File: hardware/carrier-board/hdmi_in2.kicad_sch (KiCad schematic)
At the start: 0 parts

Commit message: Integrate real downloaded component libraries; place first symbols
User downloaded SnapEDA exports for TXS0102DCUR and SS5-80-3.50-L-D-K-TR
(the level translator and SOM B2B connector selected in
carrier-board-spec.md). Extracted into hardware/carrier-board/libs/
(symbols, footprints, STEP models), re-validated every symbol and
footprint through kicad-cli sym/fp upgrade before trusting them, and
wired them into the project via sym-lib-table/fp-lib-table (with
name-aliased footprint entries matching what's baked into each
downloaded symbol's Footprint property).

Placed TXS0102DCUR in all 4 relevant sheets (hdmi_in1-3, hdmi_out) --
caught and fixed a real bug in the process (nested sub-symbol name
needs the bare "PART_0_0" form, not "LIB:PART_0_0" -- the first attempt
failed to load entirely). Also fixed grid-off-placement and a
lib_symbol_mismatch (embedded copies were missing several properties
present in the source library) once ERC surfaced them. Full-hierarchy
ERC now shows only expected "pin not connected" warnings across all
4 sheets -- correct for placed-but-unwired components, no structural
errors.

Placed J1 of the SS5 connector (160 pins, 2-unit symbol) in
som_connector.kicad_sch. Hit a real, narrower limit here: kicad-cli's
non-interactive upgrade collapses both unit instances to "unit 1"
during normalization. Verified this doesn't lose or duplicate any pin
data (160 unique pins, correctly mapped) -- it's a cosmetic/organizational
quirk in headless multi-unit handling, not a netlist bug -- but
couldn't resolve it further without the interactive GUI's purpose-built
multi-unit placement tools. Flagged in the README for the user to check
in real KiCad before J2-J4 get placed the same way.

Si5341A, ESD8040, and the Amphenol HDMI connector still need
hand-transcription from datasheets -- no pre-made libraries found for
those. README updated with full current status and next steps.
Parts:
- added U1: TXS0102DCUR, TXS0102DCUR:SOP50P310X90-8N, symbol TXS0102DCUR:TXS0102DCUR
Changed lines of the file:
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@@
 		(title "OpenAVSwitch Carrier Board - HDMI Input 2")
 		(company "OpenAVSwitch")
-		(comment 1 "Stub sheet -- not yet populated, see docs/carrier-board-spec.md")
+		(comment 1 "DDC/HPD level translator placed (TXS0102DCUR). TMDS/connector/ESD/EDID still to add.")
+	)
+	(symbol
+		(lib_id "TXS0102DCUR:TXS0102DCUR")
+		(at 99.06 99.06 0)
+		(unit 1)
+		(body_style 1)
+		(exclude_from_sim no)
+		(in_bom yes)
+		(on_board yes)
+		(in_pos_files yes)
+		(dnp no)
+		(property "Reference" "U1"
+			(at 100 80 0)
+			(show_name no)
+			(do_not_autoplace no)
+			(effects
+				(font
+					(size 1.27 1.27)
+				)
+			)
+		)
+		(property "Value" "TXS0102DCUR"
+			(at 100 122 0)
+			(show_name no)
+			(do_not_autoplace no)
+			(effects
+				(font
+					(size 1.27 1.27)
+				)
+			)
+		)
+		(property "Footprint" "TXS0102DCUR:SOP50P310X90-8N"
+			(at 99.06 99.06 0)
+			(hide yes)
+			(show_name no)
+			(do_not_autoplace no)
+			(effects
+				(font
+					(size 1.27 1.27)
+				)
+			)
+		)
+		(property "Datasheet" ""
+			(at 99.06 99.06 0)
+			(show_name no)
+			(do_not_autoplace no)
+			(effects
+				(font
+					(size 1.27 1.27)
+				)
+			)
+		)
+		(property "Description" ""
+			(at 99.06 99.06 0)
+			(show_name no)
+			(do_not_autoplace no)
+			(effects
+				(font
+					(size 1.27 1.27)
+				)
+			)
+		)
+		(pin "1"
+		)
+		(pin "2"
+		)
+		(pin "3"
+		)
+		(pin "4"
+		)
+		(pin "5"
+		)
+		(pin "6"
+		)
+		(pin "7"
+		)
+		(pin "8"
+		)
 	)
 	(sheet_instances

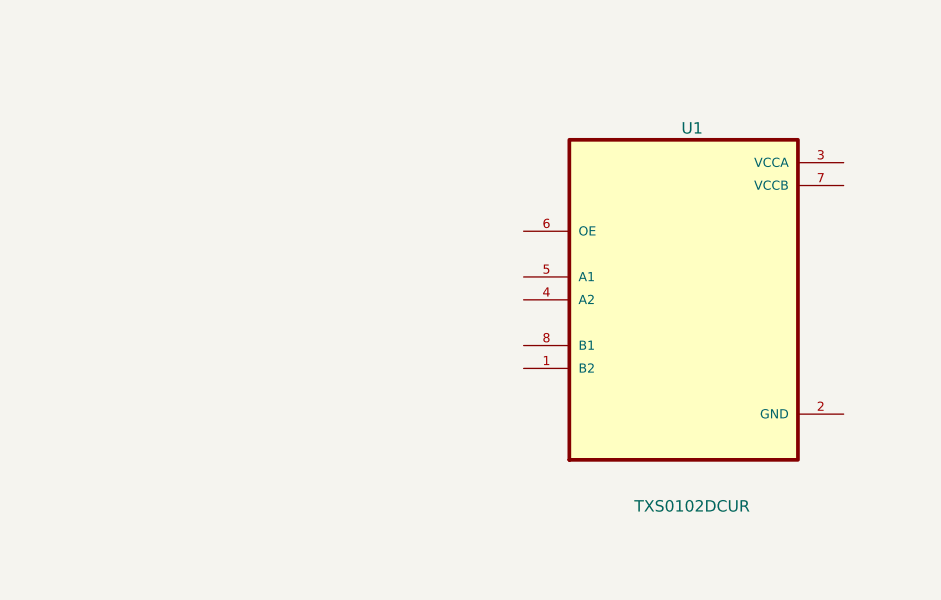
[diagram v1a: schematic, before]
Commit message: Place HDMI connector and wire TXS0102 power pins in all 4 HDMI sheets
Adds the resolved HDMI_TypeA_Receptacle (real Amphenol footprint) to
hdmi_in1-3/hdmi_out, and wires each TXS0102DCUR's VCCA/VCCB/GND to
+3V3/GND via global labels (same label-coincidence technique used in
power.kicad_sch).

Caught and fixed a real bug along the way: the local-to-global pin
coordinate transform needs global_y = base_y - local_y (KiCad flips
symbol-editor Y on placement), not +. Getting it backwards silently
swapped which net the GND and VCCB pins joined instead of failing
loudly. Also documents a kicad-cli sch erc engine quirk (traversal-
order false positive on HDMI Input 1's VCCA/GND, isolated by swapping
sheet-file references) that is not a real wiring defect.
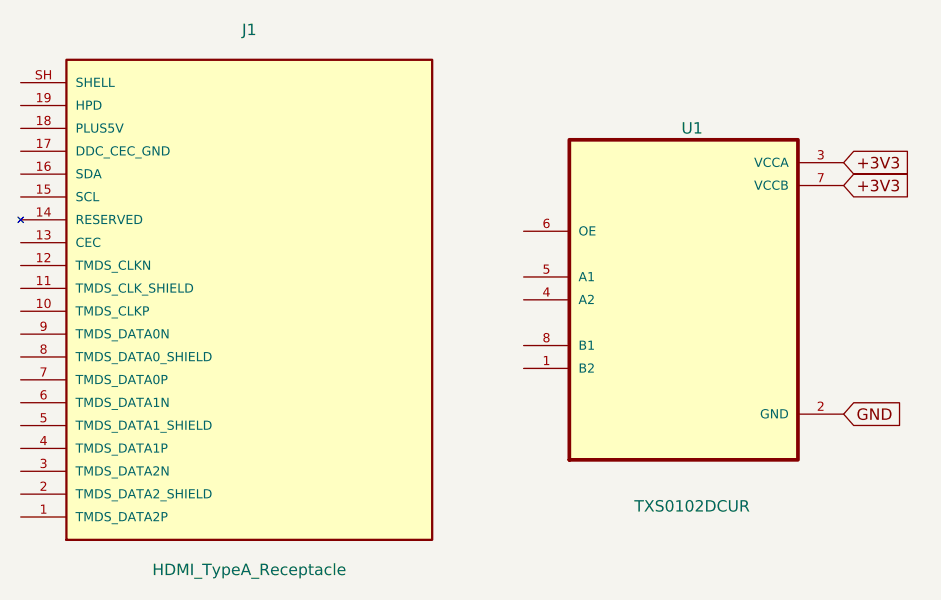
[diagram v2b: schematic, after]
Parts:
- added J1: HDMI_TypeA_Receptacle, carrier_footprints:HDMI_A_Amphenol_10029449-x01xLF_Horizontal, symbol HDMI_TypeA_Receptacle:HDMI_TypeA_Receptacle
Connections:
- net GND: now reaches U1.2 (GND)
- net +3V3: now reaches U1.3 (VCCA)
- net +3V3: now also U1.7 (VCCB)
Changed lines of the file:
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@@
 		(comment 1 "DDC/HPD level translator placed (TXS0102DCUR). TMDS/connector/ESD/EDID still to add.")
+	)
+	(global_label "GND"
+		(shape input)
+		(at 116.84 111.76 0)
+		(fields_autoplaced yes)
+		(effects
+			(font
+				(size 1.27 1.27)
+			)
+			(justify left)
+		)
+		(property "Intersheetrefs" "${INTERSHEET_REFS}"
+			(at 116.84 111.76 0)
+			(hide yes)
+			(show_name no)
+			(do_not_autoplace no)
+			(effects
+				(font
+					(size 1.27 1.27)
+				)
+			)
+		)
+	)
+	(global_label "+3V3"
+		(shape input)
+		(at 116.84 83.82 0)
+		(fields_autoplaced yes)
+		(effects
+			(font
+				(size 1.27 1.27)
+			)
+			(justify left)
+		)
+		(property "Intersheetrefs" "${INTERSHEET_REFS}"
+			(at 116.84 83.82 0)
+			(hide yes)
+			(show_name no)
+			(do_not_autoplace no)
+			(effects
+				(font
+					(size 1.27 1.27)
+				)
+			)
+		)
+	)
+	(global_label "+3V3"
+		(shape input)
+		(at 116.84 86.36 0)
+		(fields_autoplaced yes)
+		(effects
+			(font
+				(size 1.27 1.27)
+			)
+			(justify left)
+		)
+		(property "Intersheetrefs" "${INTERSHEET_REFS}"
+			(at 116.84 86.36 0)
+			(hide yes)
+			(show_name no)
+			(do_not_autoplace no)
+			(effects
+				(font
+					(size 1.27 1.27)
+				)
+			)
+		)
 	)
 	(symbol
@@
 		)
 	)
+	(symbol
+		(lib_id "HDMI_TypeA_Receptacle:HDMI_TypeA_Receptacle")
+		(at 50.8 99.06 0)
+		(unit 1)
+		(body_style 1)
+		(exclude_from_sim no)
+		(in_bom yes)
+		(on_board yes)
+		(in_pos_files yes)
+		(dnp no)
+		(property "Reference" "J1"
+			(at 50.8 69.06 0)
+			(show_name no)
+			(do_not_autoplace no)
+			(effects
+				(font
+					(size 1.27 1.27)
+				)
+			)
+		)
+		(property "Value" "HDMI_TypeA_Receptacle"
+			(at 50.8 129.06 0)
+			(show_name no)
+			(do_not_autoplace no)
+			(effects
+				(font
+					(size 1.27 1.27)
+				)
+			)
+		)
+		(property "Footprint" "carrier_footprints:HDMI_A_Amphenol_10029449-x01xLF_Horizontal"
+			(at 50.8 99.06 0)
+			(hide yes)
+			(show_name no)
+			(do_not_autoplace no)
+			(effects
+				(font
+					(size 1.27 1.27)
+				)
+			)
+		)
+		(property "Datasheet" ""
+			(at 50.8 99.06 0)
+			(show_name no)
+			(do_not_autoplace no)
+			(effects
+				(font
+					(size 1.27 1.27)
+				)
+			)
+		)
+		(property "Description" ""
+			(at 50.8 99.06 0)
+			(show_name no)
+			(do_not_autoplace no)
+			(effects
+				(font
+					(size 1.27 1.27)
+				)
+			)
+		)
+		(pin "1"
+		)
+		(pin "2"
+		)
+		(pin "3"
+		)
+		(pin "4"
+		)
+		(pin "5"
+		)
+		(pin "6"
+		)
+		(pin "7"
+		)
+		(pin "8"
+		)
+		(pin "9"
+		)
+		(pin "10"
+		)
+		(pin "11"
+		)
+		(pin "12"
+		)
+		(pin "13"
+		)
+		(pin "14"
+		)
+		(pin "15"
+		)
+		(pin "16"
+		)
+		(pin "17"
+		)
+		(pin "18"
+		)
+		(pin "19"
+		)
+		(pin "SH"
+		)
+	)

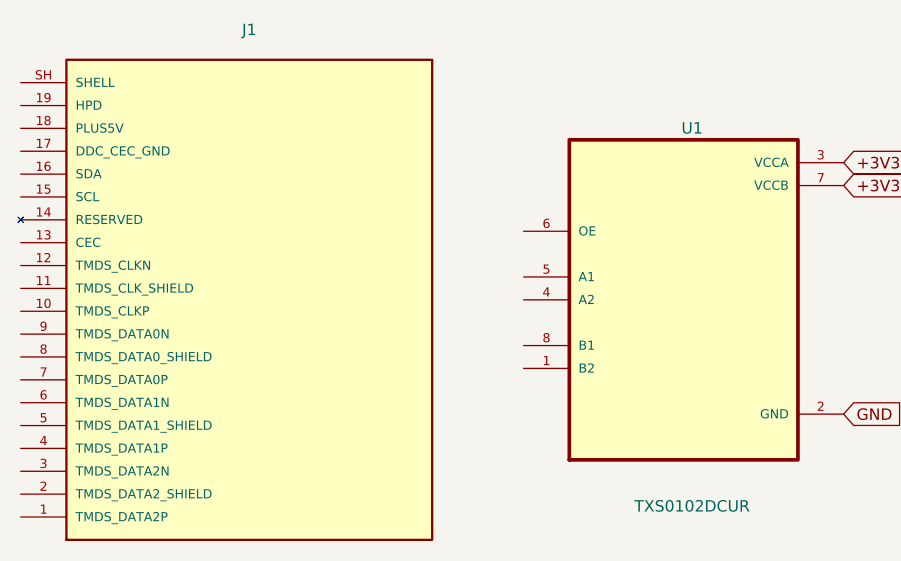
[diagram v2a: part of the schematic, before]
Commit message: Wire DDC (SCL/SDA) signal path from HDMI connector through level translator
Connects J1 pins 15/16 (SCL/SDA) to TXS0102DCUR's A-side (5V) pins via
real wires, and the B-side (3.3V) pins to per-sheet-unique global
labels (HDMI_IN1_SCL_3V3 etc) so each HDMI port's DDC bus stays
electrically independent once routed on to the SOM connector's I2C
pins. Used the corrected local-to-global pin transform documented in
the previous commit; verified by checking ERC violation coordinates
match the intended pins, not just that violation counts dropped.

HPD remains an open design decision (noted in carrier-board-spec.md)
since both TXS0102 channels are now committed to DDC.
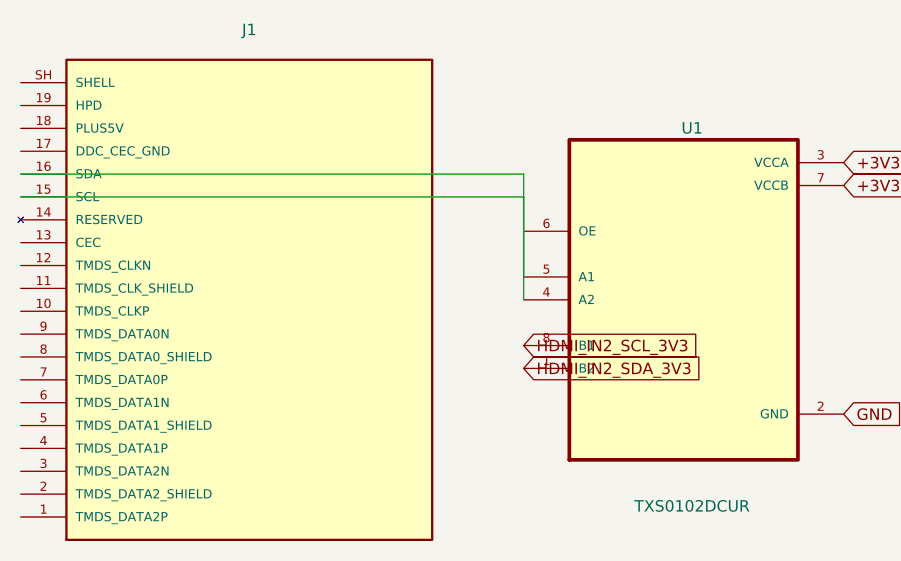
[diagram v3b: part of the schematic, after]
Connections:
- net HDMI_IN2_SDA_3V3: now reaches U1.1 (B2)
- net at U1.4 (A2): now also J1.15 (SCL), J1.16 (SDA), U1.5 (A1)
- net HDMI_IN2_SCL_3V3: now reaches U1.8 (B1)
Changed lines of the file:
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@@
 		(comment 1 "DDC/HPD level translator placed (TXS0102DCUR). TMDS/connector/ESD/EDID still to add.")
+	)
+	(wire
+		(pts
+			(xy 25.4 87.63) (xy 81.28 87.63)
+		)
+		(stroke
+			(width 0)
+			(type default)
+		)
+	)
+	(wire
+		(pts
+			(xy 81.28 87.63) (xy 81.28 96.52)
+		)
+		(stroke
+			(width 0)
+			(type default)
+		)
+	)
+	(wire
+		(pts
+			(xy 81.28 85.09) (xy 81.28 99.06)
+		)
+		(stroke
+			(width 0)
+			(type default)
+		)
+	)
+	(wire
+		(pts
+			(xy 25.4 85.09) (xy 81.28 85.09)
+		)
+		(stroke
+			(width 0)
+			(type default)
+		)
 	)
 	(global_label "GND"
@@
 		(property "Intersheetrefs" "${INTERSHEET_REFS}"
 			(at 116.84 111.76 0)
+			(hide yes)
+			(show_name no)
+			(do_not_autoplace no)
+			(effects
+				(font
+					(size 1.27 1.27)
+				)
+			)
+		)
+	)
+	(global_label "HDMI_IN2_SDA_3V3"
+		(shape input)
+		(at 81.28 106.68 0)
+		(fields_autoplaced yes)
+		(effects
+			(font
+				(size 1.27 1.27)
+			)
+			(justify left)
+		)
+		(property "Intersheetrefs" "${INTERSHEET_REFS}"
+			(at 81.28 106.68 0)
 			(hide yes)
 			(show_name no)
@@
 			(hide yes)
 			(show_name no)
+			(do_not_autoplace no)
+			(effects
+				(font
+					(size 1.27 1.27)
+				)
+			)
+		)
+	)
+	(global_label "HDMI_IN2_SCL_3V3"
+		(shape input)
+		(at 81.28 104.14 0)
+		(fields_autoplaced yes)
+		(effects
+			(font
+				(size 1.27 1.27)
+			)
+			(justify left)
+		)
+		(property "Intersheetrefs" "${INTERSHEET_REFS}"
+			(at 81.28 104.14 0)
+			(hide yes)
+			(show_name no)

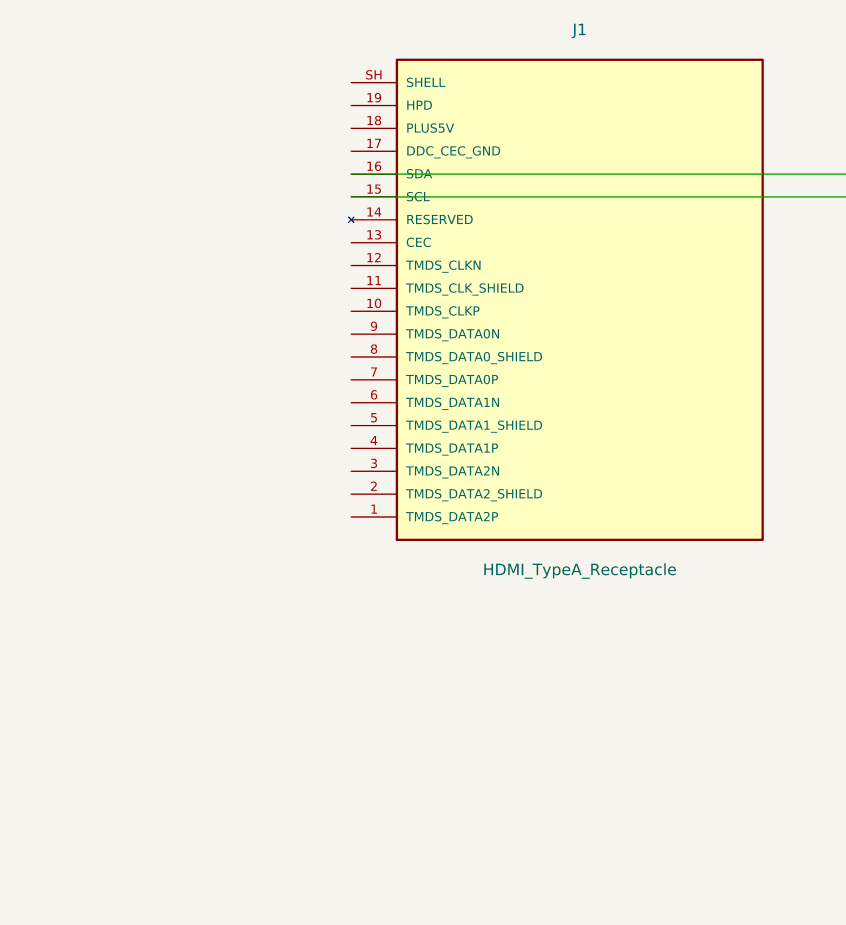
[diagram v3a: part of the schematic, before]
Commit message: Wire HPD via dedicated 2N7002 open-drain pulldown in all 4 HDMI sheets
Resolves the open HPD design question from carrier-board-spec.md:
since both TXS0102 channels are committed to DDC, HPD gets its own
simple circuit rather than double-duty on the level translator. Adds
a real 2N7002 N-MOSFET (KiCad's own Q_NMOS body, pin numbers remapped
to the real SOT-23 pinout, cross-checked against 4 independent
manufacturer datasheets) as an open-drain pulldown: J1 HPD -> Drain,
GND -> Source, a per-sheet-unique GPIO net -> Gate. No pull-up needed
on our side since the HDMI source provides it per spec.

Hit and fixed two bugs along the way, both documented in README.md:
a lib_symbols insertion script that used a fixed text marker which
silently matched the wrong location once earlier tasks changed the
surrounding file structure (fixed with brace-depth parsing instead),
and a plain grid-misalignment slip caught by the endpoint_off_grid
ERC check.
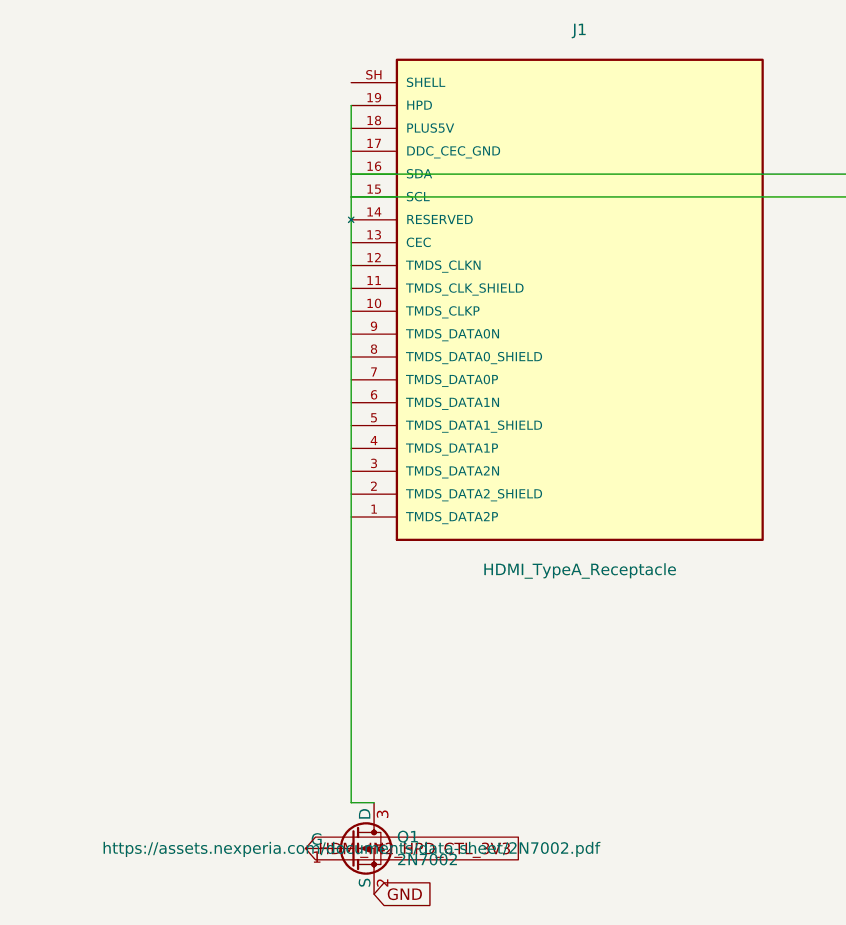
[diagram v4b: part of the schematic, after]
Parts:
- added Q1: 2N7002, carrier_footprints:SOT-23, symbol 2N7002:2N7002
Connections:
- net GND: now also Q1.2 (S)
- net at J1.19 (HPD): now also Q1.3 (D)
- new net HDMI_IN2_HPD_CTL_3V3: Q1.1 (G)
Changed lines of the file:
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@@
+	(wire
+		(pts
+			(xy 25.4 77.47) (xy 25.4 154.94)
+		)
+		(stroke
+			(width 0)
+			(type default)
+		)
+	)
 	(wire
 		(pts
@@
 	(wire
 		(pts
+			(xy 25.4 154.94) (xy 27.94 154.94)
+		)
+		(stroke
+			(width 0)
+			(type default)
+		)
+	)
+	(wire
+		(pts
 			(xy 81.28 87.63) (xy 81.28 96.52)
 		)
@@
 		(property "Intersheetrefs" "${INTERSHEET_REFS}"
 			(at 116.84 86.36 0)
+			(hide yes)
+			(show_name no)
+			(do_not_autoplace no)
+			(effects
+				(font
+					(size 1.27 1.27)
+				)
+			)
+		)
+	)
+	(global_label "GND"
+		(shape input)
+		(at 27.94 165.1 0)
+		(fields_autoplaced yes)
+		(effects
+			(font
+				(size 1.27 1.27)
+			)
+			(justify left)
+		)
+		(property "Intersheetrefs" "${INTERSHEET_REFS}"
+			(at 27.94 165.1 0)
+			(hide yes)
+			(show_name no)
+			(do_not_autoplace no)
+			(effects
+				(font
+					(size 1.27 1.27)
+				)
+			)
+		)
+	)
+	(global_label "HDMI_IN2_HPD_CTL_3V3"
+		(shape input)
+		(at 20.32 160.02 0)
+		(fields_autoplaced yes)
+		(effects
+			(font
+				(size 1.27 1.27)
+			)
+			(justify left)
+		)
+		(property "Intersheetrefs" "${INTERSHEET_REFS}"
+			(at 20.32 160.02 0)
 			(hide yes)
 			(show_name no)
@@
 		)
 	)
+	(symbol
+		(lib_id "2N7002:2N7002")
+		(at 25.4 160.02 0)
+		(unit 1)
+		(body_style 1)
+		(exclude_from_sim no)
+		(in_bom yes)
+		(on_board yes)
+		(in_pos_files yes)
+		(dnp no)
+		(property "Reference" "Q1"
+			(at 30.48 158.75 0)
+			(show_name no)
+			(do_not_autoplace no)
+			(effects
+				(font
+					(size 1.27 1.27)
+				)
+				(justify left)
+			)
+		)
+		(property "Value" "2N7002"
+			(at 30.48 161.29 0)
+			(show_name no)
+			(do_not_autoplace no)
+			(effects
+				(font
+					(size 1.27 1.27)
+				)
+				(justify left)
+			)
+		)
+		(property "Footprint" "carrier_footprints:SOT-23"
+			(at 25.4 160.02 0)
+			(hide yes)
+			(show_name no)
+			(do_not_autoplace no)
+			(effects
+				(font
+					(size 1.27 1.27)
+				)
+			)
+		)
+		(property "Datasheet" "https://assets.nexperia.com/documents/data-sheet/2N7002.pdf"
+			(at 25.4 160.02 0)
+			(show_name no)
+			(do_not_autoplace no)
+			(effects
+				(font
+					(size 1.27 1.27)
+				)
+			)
+		)
+		(property "Description" ""
+			(at 25.4 160.02 0)
+			(show_name no)
+			(do_not_autoplace no)
+			(effects
+				(font
+					(size 1.27 1.27)
+				)
+			)
+		)
+		(pin "1"
+		)
+		(pin "2"
+		)
+		(pin "3"
+		)
+	)
